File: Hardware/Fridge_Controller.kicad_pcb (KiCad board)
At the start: 2 copper layers, 91 x 67 mm, 22 parts, among them J1 CTB0508/2, J2 CTB0508/2, J3 CTB0508/2, K1 RZ01-1A4-D005, Q1 DMG3414U, U1 PIC12F683-IP, U2 MCP1541T-ITT

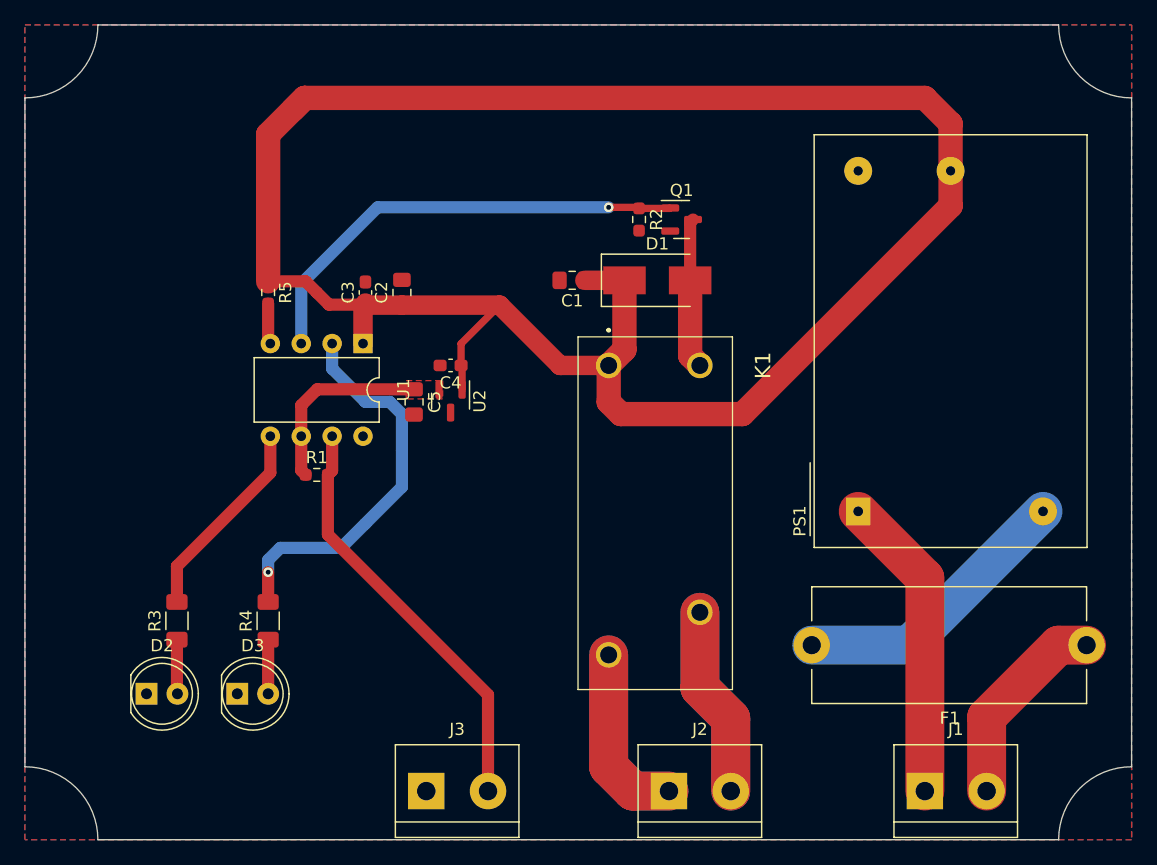
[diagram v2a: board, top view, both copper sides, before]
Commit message: [Hardware] Cleaned all PCB warnings.
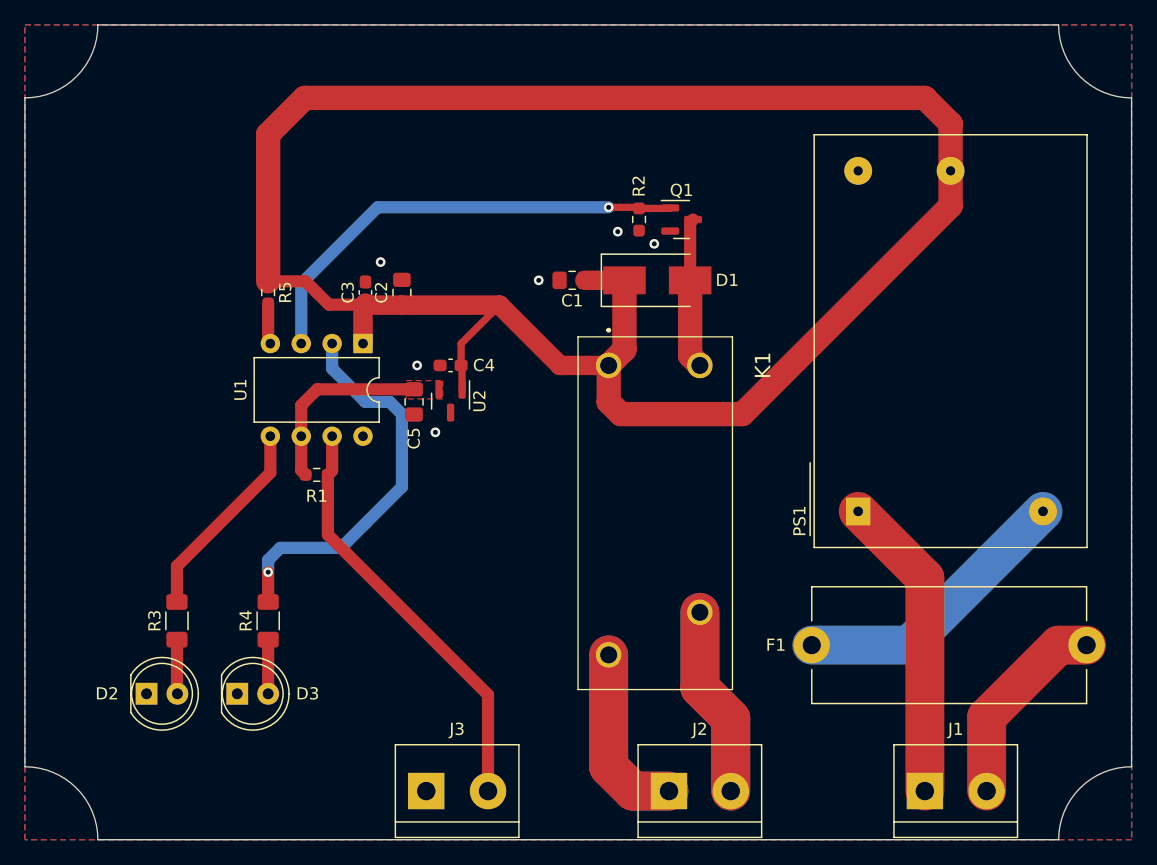
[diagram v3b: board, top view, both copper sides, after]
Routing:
- net +5V: track 170.5 -> 169.1 mm
- net GND: vias 0 -> 6
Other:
- board text added: "2022-12-27"
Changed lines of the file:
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@@
     (property "Sheetname" "")
     (attr through_hole)
-    (fp_text reference "D2" (at 1.27 -3.96) (layer "F.SilkS")
+    (fp_text reference "D2" (at -3.25 0) (layer "F.SilkS")
       (effects (font (size 1 1) (thickness 0.15)))
     )
@@
     (property "Value2" "1%")
     (attr smd)
-    (fp_text reference "R1" (at 0 -1.43) (layer "F.SilkS")
+    (fp_text reference "R1" (at 0 1.75) (layer "F.SilkS")
       (effects (font (size 1 1) (thickness 0.15)))
     )
@@
     (property "Sheetname" "")
     (attr through_hole)
-    (fp_text reference "U1" (at 3.81 -3.33 90) (layer "F.SilkS")
+    (fp_text reference "U1" (at 3.81 10.05 90) (layer "F.SilkS")
       (effects (font (size 1 1) (thickness 0.15)))
     )
@@
     (property "Value2" "1%")
     (attr smd)
-    (fp_text reference "R2" (at 0 -1.43 90) (layer "F.SilkS")
+    (fp_text reference "R2" (at -2.75 0 90) (layer "F.SilkS")
       (effects (font (size 1 1) (thickness 0.15)))
     )
@@
     (property "Sheetname" "")
     (attr smd)
-    (fp_text reference "D1" (at 0 -3) (layer "F.SilkS")
+    (fp_text reference "D1" (at 5.75 0) (layer "F.SilkS")
       (effects (font (size 1 1) (thickness 0.15)))
     )
@@
     (property "Value3" "X7R")
     (attr smd)
-    (fp_text reference "C4" (at 0 -1.43) (layer "F.SilkS")
+    (fp_text reference "C4" (at -2.75 0) (layer "F.SilkS")
       (effects (font (size 1 1) (thickness 0.15)))
     )
@@
     (property "Value3" "X7R")
     (attr smd)
-    (fp_text reference "C5" (at 0 -1.68 90) (layer "F.SilkS")
+    (fp_text reference "C5" (at 3 0 90) (layer "F.SilkS")
       (effects (font (size 1 1) (thickness 0.15)))
     )
@@
     (property "Sheetname" "")
     (attr through_hole)
-    (fp_text reference "D3" (at 1.27 -3.96) (layer "F.SilkS")
+    (fp_text reference "D3" (at 5.79 0) (layer "F.SilkS")
       (effects (font (size 1 1) (thickness 0.15)))
     )
@@
     (property "Value2" "250V-2A-T")
     (attr through_hole)
-    (fp_text reference "F1" (at 11.25 -6) (layer "F.SilkS")
+    (fp_text reference "F1" (at 25.55 0) (layer "F.SilkS")
       (effects (font (size 1 1) (thickness 0.15)))
     )
@@
   (gr_arc (start 191 79) (mid 186.757359 77.242641) (end 185 73) (layer "Edge.Cuts") (width 0.1))
   (gr_arc (start 100 134) (mid 104.242641 135.757359) (end 106 140) (layer "Edge.Cuts") (width 0.1))
-  (dimension (type aligned) (layer "Edge.Cuts")
-    (pts (xy 168 140) (xy 163 140))
-    (height -12)
-    (gr_text "5,0000 mm" (at 165.5 150.85) (layer "Edge.Cuts")
-      (effects (font (size 1 1) (thickness 0.15)))
-    )
-    (format (units 3) (units_format 1) (precision 4))
-    (style (thickness 0.1) (arrow_length 1.27) (text_position_mode 0) (extension_height 0.58642) (extension_offset 0.5) keep_text_aligned)
-  )
-  (dimension (type aligned) (layer "Edge.Cuts")
-    (pts (xy 143 140) (xy 128 140))
-    (height -8)
-    (gr_text "15,0000 mm" (at 135.5 146.85) (layer "Edge.Cuts")
-      (effects (font (size 1 1) (thickness 0.15)))
-    )
-    (format (units 3) (units_format 1) (precision 4))
-    (style (thickness 0.1) (arrow_length 1.27) (text_position_mode 0) (extension_height 0.58642) (extension_offset 0.5) keep_text_aligned)
-  )
-  (dimension (type aligned) (layer "Edge.Cuts")
-    (pts (xy 163 140) (xy 148 140))
-    (height -8)
-    (gr_text "15,0000 mm" (at 155.5 146.85) (layer "Edge.Cuts")
-      (effects (font (size 1 1) (thickness 0.15)))
-    )
-    (format (units 3) (units_format 1) (precision 4))
-    (style (thickness 0.1) (arrow_length 1.27) (text_position_mode 0) (extension_height 0.58642) (extension_offset 0.5) keep_text_aligned)
-  )
-  (dimension (type aligned) (layer "Edge.Cuts")
-    (pts (xy 148 140) (xy 143 140))
-    (height -12)
-    (gr_text "5,0000 mm" (at 145.5 150.85) (layer "Edge.Cuts")
-      (effects (font (size 1 1) (thickness 0.15)))
-    )
-    (format (units 3) (units_format 1) (precision 4))
-    (style (thickness 0.1) (arrow_length 1.27) (text_position_mode 0) (extension_height 0.58642) (extension_offset 0.5) keep_text_aligned)
-  )
-  (dimension (type aligned) (layer "Edge.Cuts")
-    (pts (xy 185 140) (xy 168 140))
-    (height -8)
-    (gr_text "17,0000 mm" (at 176.5 146.85) (layer "Edge.Cuts")
-      (effects (font (size 1 1) (thickness 0.15)))
-    )
-    (format (units 3) (units_format 1) (precision 4))
-    (style (thickness 0.1) (arrow_length 1.27) (text_position_mode 0) (extension_height 0.58642) (extension_offset 0.5) keep_text_aligned)
-  )
-  (dimension (type aligned) (layer "Edge.Cuts")
-    (pts (xy 128 140) (xy 123 140))
-    (height -12)
-    (gr_text "5,0000 mm" (at 125.5 150.85) (layer "Edge.Cuts")
-      (effects (font (size 1 1) (thickness 0.15)))
-    )
-    (format (units 3) (units_format 1) (precision 4))
-    (style (thickness 0.1) (arrow_length 1.27) (text_position_mode 0) (extension_height 0.58642) (extension_offset 0.5) keep_text_aligned)
+  (gr_text "2022-12-27" (at 109.5 94.75 90) (layer "F.Mask")
+    (effects (font (size 1.5 1.5) (thickness 0.3)))
   )
   (segment (start 127.8 96.2) (end 128 96) (width 1.6) (layer "F.Cu") (net 1))
@@
   (segment (start 176.1175 81.1175) (end 174 79) (width 2) (layer "F.Cu") (net 1))
   (segment (start 146.0375 94) (end 149.3 94) (width 1.6) (layer "F.Cu") (net 1))
-  (segment (start 123 79) (end 122 80) (width 2) (layer "F.Cu") (net 1))
   (segment (start 120 82) (end 123 79) (width 2) (layer "F.Cu") (net 1))
   (segment (start 135.8625 99.2125) (end 139.0375 96.0375) (width 0.6) (layer "F.Cu") (net 1))
+  (via (at 129.25 92.5) (size 0.8) (drill 0.4) (layers "F.Cu" "B.Cu") (free) (net 2))
+  (via (at 132.25 101) (size 0.8) (drill 0.4) (layers "F.Cu" "B.Cu") (free) (net 2))
+  (via (at 148.75 90) (size 0.8) (drill 0.4) (layers "F.Cu" "B.Cu") (free) (net 2))
+  (via (at 151.75 91) (size 0.8) (drill 0.4) (layers "F.Cu" "B.Cu") (free) (net 2))
+  (via (at 142.25 94) (size 0.8) (drill 0.4) (layers "F.Cu" "B.Cu") (free) (net 2))
+  (via (at 133.75 106.5) (size 0.8) (drill 0.4) (layers "F.Cu" "B.Cu") (free) (net 2))
   (segment (start 122.72 104.28) (end 122.72 106.82) (width 1) (layer "F.Cu") (net 3))
   (segment (start 122.72 106.82) (end 122.72 109.6325) (width 1) (layer "F.Cu") (net 3))
